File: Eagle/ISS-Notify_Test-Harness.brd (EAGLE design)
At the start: 63.5 x 63.5 mm, 31 parts, among them U1 ATMEGA32U4, U3 TPS63001, X1 8 MHz

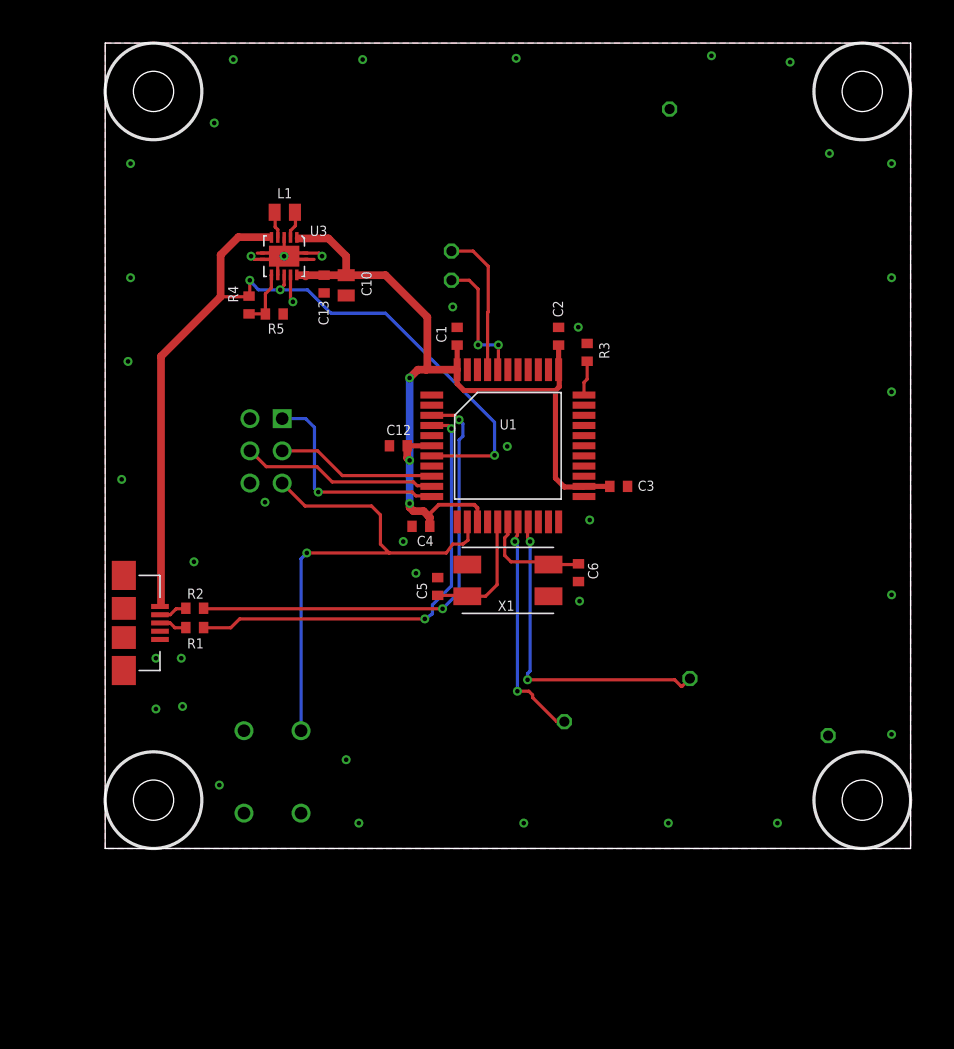
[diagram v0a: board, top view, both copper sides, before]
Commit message: pogo pin landings for test harness
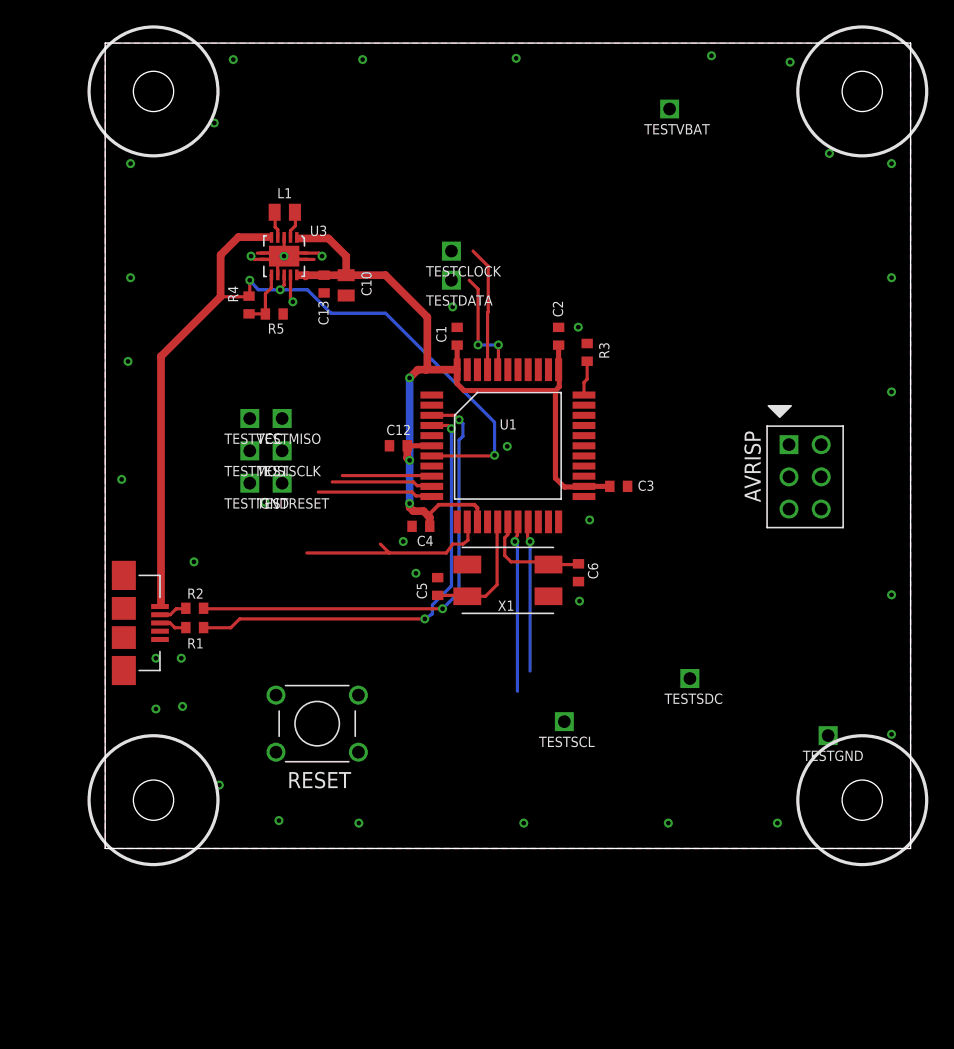
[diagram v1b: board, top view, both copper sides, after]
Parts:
- added TESTIGND, TESTMISO, TESTMOSI, TESTRESET, TESTSCLK, TESTVCC: POGOPIN, ISS-Notify:POGOPIN
- TESTCLOCK, TESTDATA, TESTGND, TESTSCL, TESTSDC, TESTVBAT: value TESTPIN -> POGOPIN; device ISS-Notify:TESTPIN -> ISS-Notify:POGOPIN
- U$1, U$2, U$3, U$4: value _4-BARE_MOUNTING_HOLE/.300 -> _4-BARE_MOUNTING_HOLE/.400; device ISS-Notify:_4/.300-BARE+STD_NUT_OR_STAR_WASHER -> ISS-Notify:_4/.400-BARE+STD_TOOL_CLEARANCE
- moved AVRISP 42.5 mm to (55.2, 29.3), flipped to the top
- moved RESET 5.19 mm to (16.7, 9.84), flipped to the top, turned to 0 degrees
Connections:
- removed net MFP: U1.21
- net GND: now also TESTGND.1, TESTIGND.1; no longer TESTGND.P$1
- net LED_CLK: now also TESTCLOCK.1; no longer TESTCLOCK.P$1
- net LED_DATA: now also TESTDATA.1; no longer TESTDATA.P$1
- net MISO: now also TESTMISO.1
- net MOSI: now also TESTMOSI.1
- net RESET: now also TESTRESET.1
- net SCL: now also TESTSCL.1; no longer TESTSCL.P$1
- net SCLK: now also TESTSCLK.1
- net SDA: now also TESTSDC.1; no longer TESTSDC.P$1
- net VIN: now also TESTVBAT.1
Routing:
- net RESET: track 40.9 -> 15.6 mm, vias 1 -> 0
- net SDA: track 25.9 -> 11.9 mm, vias 2 -> 1
- net MISO: track 17.2 -> 9.09 mm, vias 1 -> 0
- net MOSI: track 15.5 -> 7.98 mm
- net SCLK: track 12.6 -> 7.07 mm
- net SCL: track 18.3 -> 13.5 mm, vias 2 -> 1
- net LED_CLK: track 11.6 -> 9.87 mm
- net LED_DATA: track 10.4 -> 8.96 mm

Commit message: first pass routing to pogo pins on test harness
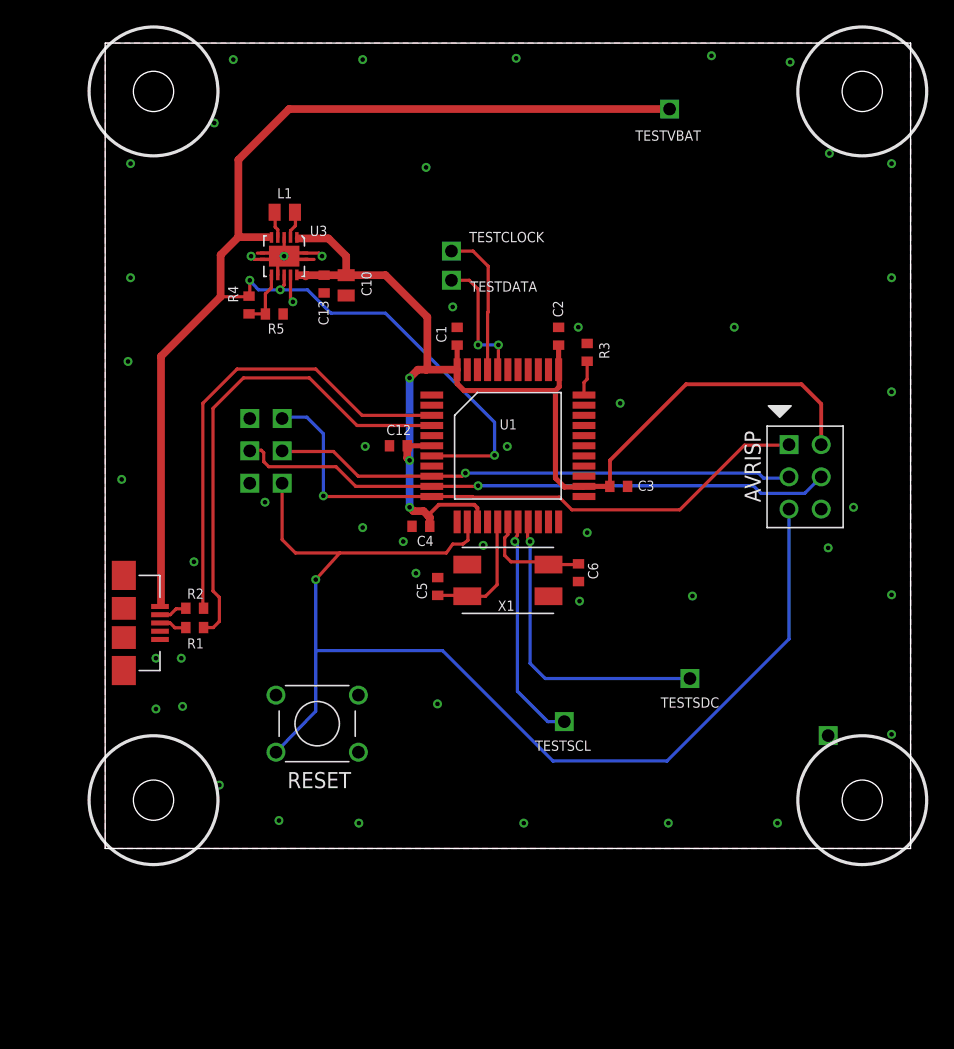
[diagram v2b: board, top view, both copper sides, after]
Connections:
- new net N$3: TESTVCC.1, U1.36
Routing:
- net RESET: track 15.6 -> 94.3 mm, vias 0 -> 1
- net VIN: track 70.8 -> 112.6 mm
- net MOSI: track 7.98 -> 47.5 mm, vias 0 -> 1
- net MISO: track 9.09 -> 48.0 mm, vias 0 -> 1
- net SCLK: track 7.07 -> 41.2 mm, vias 0 -> 1
- net VCC: track 73.7 -> 98.8 mm
- net SDA: track 11.9 -> 24.4 mm
- net SCL: track 13.5 -> 18.2 mm
- net D+: track 35.4 -> 38.2 mm, vias 2 -> 0
- net LED_CLK: track 9.87 -> 11.6 mm
- net LED_DATA: track 8.96 -> 10.4 mm
- net D-: track 36.8 -> 36.9 mm, vias 2 -> 0
- net GND: vias 39 -> 49

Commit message: clean up power supply, 6 pin header for programming test board
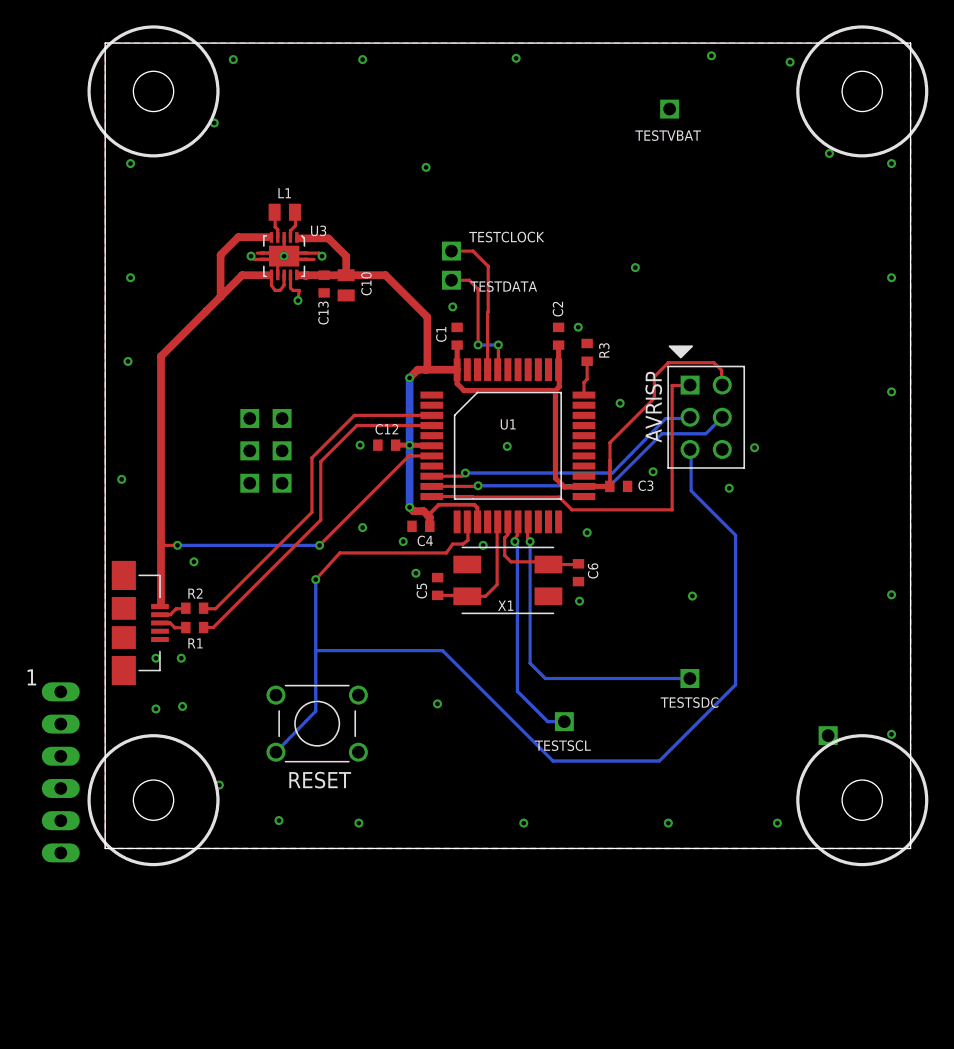
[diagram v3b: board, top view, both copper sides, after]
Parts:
- removed R4: 39 k, rcl_custom:0603-C-NOSILK
- removed R5: 51 k, rcl_custom:0603-C-NOSILK
- added J1: 6HEADER, ISS-Notify:6HEAD
- moved AVRISP 9.11 mm to (47.4, 34.0)
- moved C12 0.92 mm to (22.2, 31.8)
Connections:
- removed net BATSENSE: R4.1, R5.2, U3.6
- removed net MISO: AVRISP.1, TESTMISO.1, U1.11
- removed net MOSI: AVRISP.4, TESTMOSI.1, U1.10
- removed net N$3: TESTVCC.1, U1.36
- removed net SCLK: AVRISP.3, TESTSCLK.1, U1.9
- new net N$7: AVRISP.1, U1.11
- new net N$8: AVRISP.3, U1.9
- new net N$9: AVRISP.4, U1.10
- net GND: no longer R5.1, TESTIGND.1
- net RESET: no longer TESTRESET.1
- net VIN: now also U3.6; no longer R4.2, TESTVBAT.1
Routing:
- net MISO: track 48.0 -> 0.00 mm, vias 1 -> 0
- net MOSI: track 47.5 -> 0.00 mm, vias 1 -> 0
- net VIN: track 112.6 -> 66.8 mm, vias 3 -> 2
- net SCLK: track 41.2 -> 0.00 mm, vias 1 -> 0
- net N$7: track 0.00 -> 30.6 mm
- net N$9: track 0.00 -> 25.2 mm, vias 0 -> 1
- net N$8: track 0.00 -> 22.4 mm, vias 0 -> 1
- net D+: track 38.2 -> 27.3 mm
- net D-: track 36.9 -> 26.9 mm
- net VCC: track 98.8 -> 90.7 mm
- net RESET: track 94.3 -> 89.0 mm
- net BATSENSE: track 4.63 -> 0.00 mm

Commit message: external programmer for test board
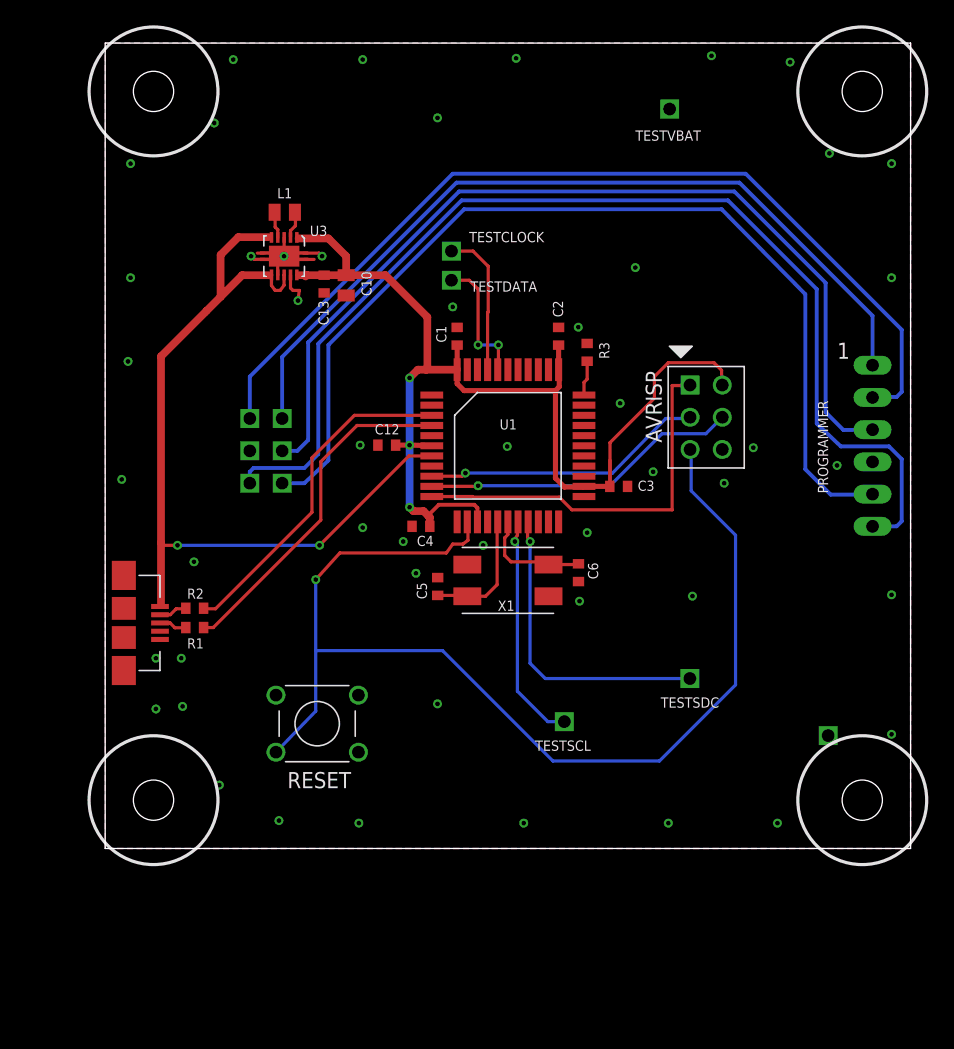
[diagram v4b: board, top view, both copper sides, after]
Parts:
- removed J1: 6HEADER, ISS-Notify:6HEAD
- added JPROGRAMER: 6HEADER, ISS-Notify:6HEAD
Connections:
- net N$7 renamed MISO
- net N$8 renamed AVRCLK
- net N$9 renamed MOSI
- new net TESTGND: JPROGRAMER.6, TESTIGND.1
- new net TESTMISO: JPROGRAMER.1, TESTMISO.1
- new net TESTMOSI: TESTMOSI.1
- new net TESTRESET: JPROGRAMER.5, TESTRESET.1
- new net TESTSCLK: JPROGRAMER.3, TESTSCLK.1
- new net TESTVCC: JPROGRAMER.2, TESTVCC.1
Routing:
- net TESTGND: track 0.00 -> 88.3 mm
- net TESTRESET: track 0.00 -> 78.2 mm
- net TESTVCC: track 0.00 -> 73.8 mm
- net TESTSCLK: track 0.00 -> 73.3 mm
- net TESTMISO: track 0.00 -> 65.3 mm
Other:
- board text added: "PROGRAMMER"
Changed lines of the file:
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@@
 <wire x1="63.5" y1="63.5" x2="0" y2="63.5" width="0" layer="20"/>
 <wire x1="0" y1="63.5" x2="0" y2="0" width="0" layer="20"/>
+<text x="57" y="28" size="0.8128" layer="25" font="vector" ratio="20" rot="R90">PROGRAMMER</text>
 </plain>
 <attributes>
@@
 <element name="TESTRESET" library="ISS-Notify" package="POGOPIN" value="POGOPIN" x="13.95" y="28.8" smashed="yes"/>
 <element name="TESTIGND" library="ISS-Notify" package="POGOPIN" value="POGOPIN" x="11.4" y="28.8" smashed="yes"/>
-<element name="J1" library="ISS-Notify" package="6HEAD" value="6HEADER" x="-3.5" y="6"/>
+<element name="JPROGRAMER" library="ISS-Notify" package="6HEAD" value="6HEADER" x="60.5" y="31.75"/>
 </elements>
 <signals>
@@
 <via x="62" y="54" extent="1-16" drill="0.36"/>
 <via x="62" y="45" extent="1-16" drill="0.36"/>
-<via x="62" y="36" extent="1-16" drill="0.36"/>
+<via x="57.7" y="30.2" extent="1-16" drill="0.36"/>
 <via x="62" y="20" extent="1-16" drill="0.36"/>
 <via x="62" y="9" extent="1-16" drill="0.36"/>
@@
 <via x="46.3" y="19.9" extent="1-16" drill="0.36"/>
 <via x="41.8" y="45.8" extent="1-16" drill="0.36"/>
-<via x="51.2" y="31.6" extent="1-16" drill="0.36"/>
-<via x="49.2" y="28.4" extent="1-16" drill="0.36"/>
-<via x="25.3" y="53.7" extent="1-16" drill="0.36"/>
+<via x="51.1" y="31.6" extent="1-16" drill="0.36"/>
+<via x="48.8" y="28.8" extent="1-16" drill="0.36"/>
+<via x="26.2" y="57.6" extent="1-16" drill="0.36"/>
 <via x="29.8" y="23.9" extent="1-16" drill="0.36"/>
 <via x="40.6" y="35.1" extent="1-16" drill="0.36"/>
@@
 <wire x1="46.2" y1="31.374" x2="46.114" y2="31.46" width="0.254" layer="16"/>
 </signal>
-<signal name="N$7">
+<signal name="MISO">
 <contactref element="AVRISP" pad="1"/>
 <contactref element="U1" pad="11"/>
@@
 <wire x1="46.074" y1="36.5" x2="46.114" y2="36.54" width="0.254" layer="1"/>
 </signal>
-<signal name="N$8">
+<signal name="AVRCLK">
 <contactref element="U1" pad="9"/>
 <contactref element="AVRISP" pad="3"/>
@@
 <wire x1="46.014" y1="33.9" x2="46.114" y2="34" width="0.254" layer="16"/>
 </signal>
-<signal name="N$9">
+<signal name="MOSI">
 <contactref element="AVRISP" pad="4"/>
 <contactref element="U1" pad="10"/>
@@
 <wire x1="47.354" y1="32.7" x2="48.654" y2="34" width="0.254" layer="16"/>
 </signal>
+<signal name="TESTMISO">
+<contactref element="JPROGRAMER" pad="1"/>
+<contactref element="TESTMISO" pad="1"/>
+<wire x1="13.95" y1="33.9" x2="13.95" y2="38.75" width="0.3048" layer="16"/>
+<wire x1="13.95" y1="38.75" x2="27.7" y2="52.5" width="0.3048" layer="16"/>
+<wire x1="27.7" y1="52.5" x2="50" y2="52.5" width="0.3048" layer="16"/>
+<wire x1="50" y1="52.5" x2="60.5" y2="42" width="0.3048" layer="16"/>
+<wire x1="60.5" y1="42" x2="60.5" y2="38.1" width="0.3048" layer="16"/>
+</signal>
+<signal name="TESTVCC">
+<contactref element="JPROGRAMER" pad="2"/>
+<contactref element="TESTVCC" pad="1"/>
+<wire x1="11.4" y1="33.9" x2="11.4" y2="37.2" width="0.3048" layer="16"/>
+<wire x1="11.4" y1="37.2" x2="27.4" y2="53.2" width="0.3048" layer="16"/>
+<wire x1="27.4" y1="53.2" x2="50.5" y2="53.2" width="0.3048" layer="16"/>
+<wire x1="50.5" y1="53.2" x2="62.8" y2="40.9" width="0.3048" layer="16"/>
+<wire x1="62.8" y1="40.9" x2="62.8" y2="36" width="0.3048" layer="16"/>
+<wire x1="62.8" y1="36" x2="62.4" y2="35.6" width="0.3048" layer="16"/>
+<wire x1="62.4" y1="35.6" x2="60.54" y2="35.6" width="0.3048" layer="16"/>
+<wire x1="60.54" y1="35.6" x2="60.5" y2="35.56" width="0.3048" layer="16"/>
+</signal>
+<signal name="TESTSCLK">
+<contactref element="JPROGRAMER" pad="3"/>
+<contactref element="TESTSCLK" pad="1"/>
+<wire x1="13.95" y1="31.35" x2="15.15" y2="31.35" width="0.3048" layer="16"/>
+<wire x1="15.15" y1="31.35" x2="16" y2="32.2" width="0.3048" layer="16"/>
+<wire x1="16" y1="32.2" x2="16" y2="39.9" width="0.3048" layer="16"/>
+<wire x1="16" y1="39.9" x2="27.9" y2="51.8" width="0.3048" layer="16"/>
+<wire x1="27.9" y1="51.8" x2="49.6" y2="51.8" width="0.3048" layer="16"/>
+<wire x1="49.6" y1="51.8" x2="56.8" y2="44.6" width="0.3048" layer="16"/>
+<wire x1="56.8" y1="44.6" x2="56.8" y2="34.4" width="0.3048" layer="16"/>
+<wire x1="56.8" y1="34.4" x2="58.2" y2="33" width="0.3048" layer="16"/>
+<wire x1="58.2" y1="33" x2="60.48" y2="33" width="0.3048" layer="16"/>
+<wire x1="60.48" y1="33" x2="60.5" y2="33.02" width="0.3048" layer="16"/>
+</signal>
+<signal name="TESTMOSI">
+<contactref element="TESTMOSI" pad="1"/>
+</signal>
+<signal name="TESTRESET">
+<contactref element="JPROGRAMER" pad="5"/>
+<contactref element="TESTRESET" pad="1"/>
+<wire x1="13.95" y1="28.8" x2="15.7" y2="28.8" width="0.3048" layer="16"/>
+<wire x1="15.7" y1="28.8" x2="17.6" y2="30.6" width="0.3048" layer="16"/>
+<wire x1="17.6" y1="30.6" x2="17.6" y2="39.7" width="0.3048" layer="16"/>
+<wire x1="17.6" y1="39.7" x2="28.3" y2="50.4" width="0.3048" layer="16"/>
+<wire x1="28.3" y1="50.4" x2="48.6" y2="50.4" width="0.3048" layer="16"/>
+<wire x1="48.6" y1="50.4" x2="55.2" y2="43.7" width="0.3048" layer="16"/>
+<wire x1="55.2" y1="43.7" x2="55.2" y2="29.9" width="0.3048" layer="16"/>
+<wire x1="55.2" y1="29.9" x2="57.2" y2="27.9" width="0.3048" layer="16"/>
+<wire x1="57.2" y1="27.9" x2="60.46" y2="27.9" width="0.3048" layer="16"/>
+<wire x1="60.46" y1="27.9" x2="60.5" y2="27.94" width="0.3048" layer="16"/>
+</signal>
+<signal name="TESTGND">
+<contactref element="JPROGRAMER" pad="6"/>
+<contactref element="TESTIGND" pad="1"/>
+<wire x1="11.4" y1="28.8" x2="11.4" y2="29.7" width="0.3048" layer="16"/>
+<wire x1="11.4" y1="29.7" x2="11.7" y2="30" width="0.3048" layer="16"/>
+<wire x1="11.7" y1="30" x2="15.7" y2="30" width="0.3048" layer="16"/>
+<wire x1="15.7" y1="30" x2="16.8" y2="31.1" width="0.3048" layer="16"/>
+<wire x1="16.8" y1="31.1" x2="16.8" y2="39.8" width="0.3048" layer="16"/>
+<wire x1="16.8" y1="39.8" x2="28.1" y2="51.1" width="0.3048" layer="16"/>
+<wire x1="28.1" y1="51.1" x2="49.1" y2="51.1" width="0.3048" layer="16"/>
+<wire x1="49.1" y1="51.1" x2="56.1" y2="44.1" width="0.3048" layer="16"/>
+<wire x1="56.1" y1="44.1" x2="56.1" y2="33.5" width="0.3048" layer="16"/>
+<wire x1="56.1" y1="33.5" x2="58" y2="31.7" width="0.3048" layer="16"/>
+<wire x1="58" y1="31.7" x2="61.8" y2="31.7" width="0.3048" layer="16"/>
+<wire x1="61.8" y1="31.7" x2="62.8" y2="30.7" width="0.3048" layer="16"/>
+<wire x1="62.8" y1="30.7" x2="62.8" y2="25.8" width="0.3048" layer="16"/>
+<wire x1="62.8" y1="25.8" x2="62.4" y2="25.4" width="0.3048" layer="16"/>
+<wire x1="62.4" y1="25.4" x2="60.5" y2="25.4" width="0.3048" layer="16"/>
+</signal>
 </signals>
